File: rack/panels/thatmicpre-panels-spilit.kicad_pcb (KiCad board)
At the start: 2 copper layers, 87.9 x 78 mm, 2 parts

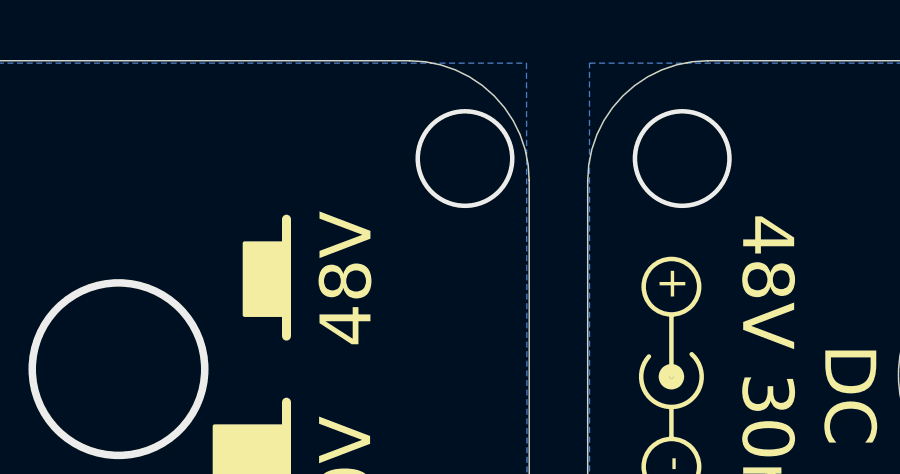
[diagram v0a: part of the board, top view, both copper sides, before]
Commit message: Fixed the issue where one hole on the front panel was offset by 1mm from its correct position.
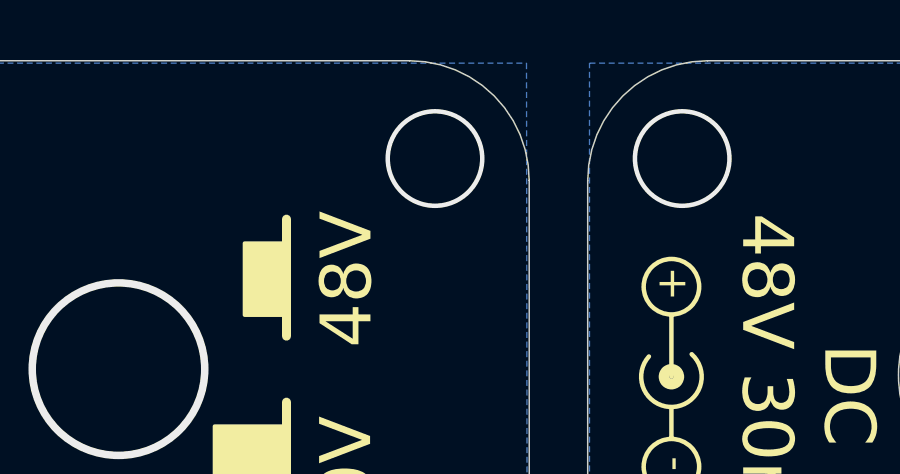
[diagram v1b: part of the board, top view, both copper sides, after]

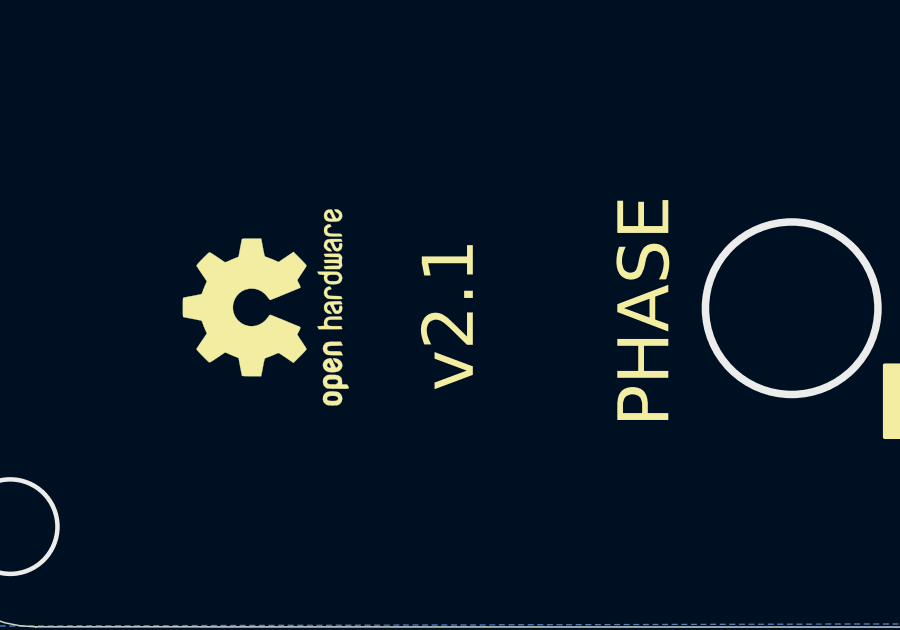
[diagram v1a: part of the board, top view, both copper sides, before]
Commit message: Added a pad on the front panel for connecting GND to the enclosure.
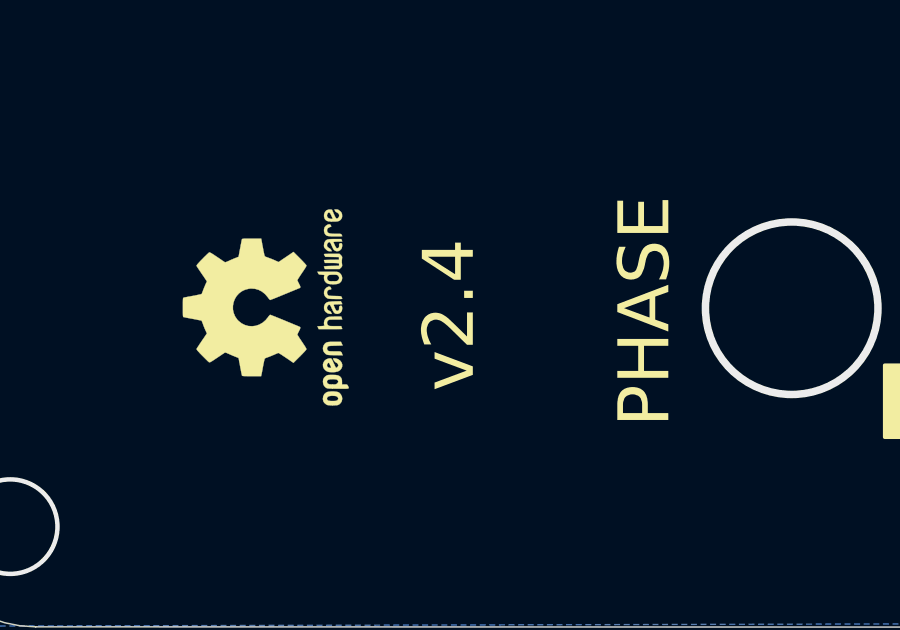
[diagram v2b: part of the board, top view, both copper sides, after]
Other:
- board text added: "v2.4"
- board text removed: "v2.1"
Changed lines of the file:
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@@
 		(embedded_fonts no)
+	)
+	(gr_rect
+		(start 134.05 108.7)
+		(end 138.05 112.7)
+		(stroke
+			(width 0.2)
+			(type solid)
+		)
+		(fill yes)
+		(layers "B.Cu" "B.Mask")
+		(net "GND")
 	)
 	(gr_circle
@@
 		)
 	)
-	(gr_text "v2.1"
+	(gr_text "v2.4"
 		(at 120.4722 122.0216 90)
 		(layer "F.SilkS")
